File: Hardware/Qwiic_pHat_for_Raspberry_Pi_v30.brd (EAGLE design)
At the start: 65 x 30.5 mm, 46 parts, among them J1 RASPBERRYPI-40-PIN-GPIO_PTH_N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, J4 Qwiic Right Angle, J7 Qwiic Right Angle

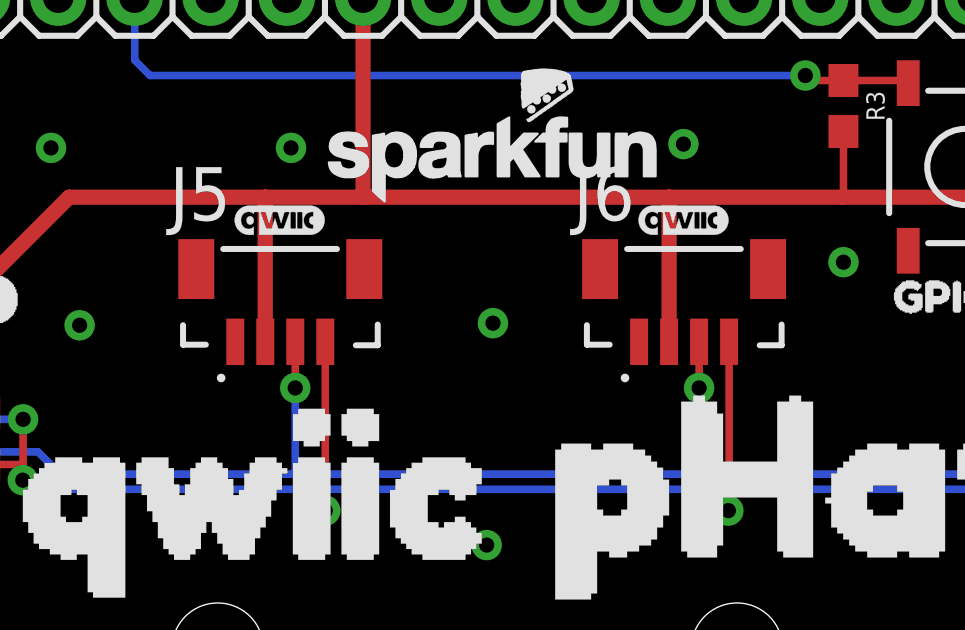
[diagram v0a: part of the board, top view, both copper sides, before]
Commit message: Fixes vertical qwiic connector polarity marker with updated package, removes Qwiic board reference on TDocu
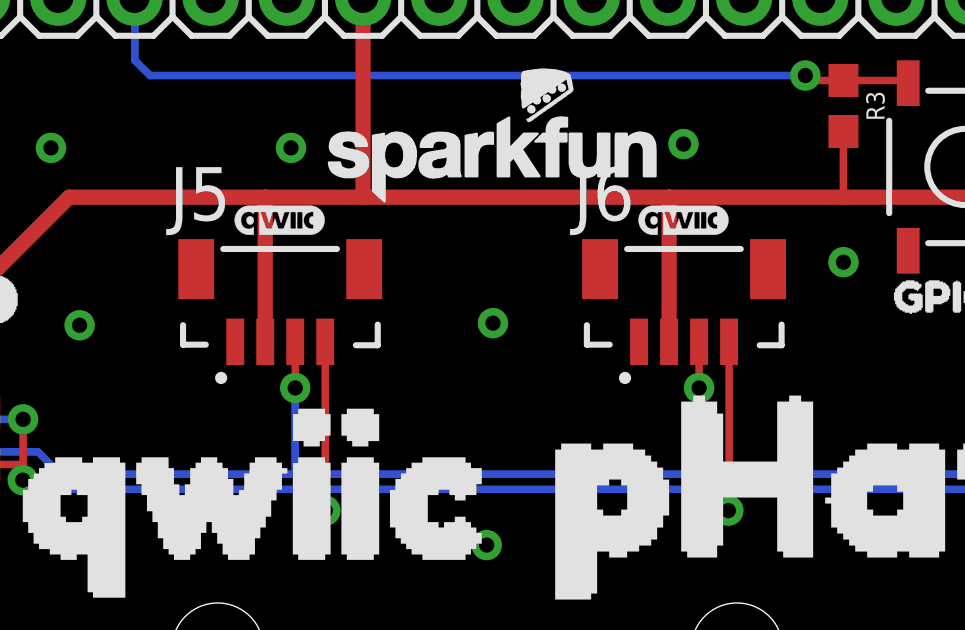
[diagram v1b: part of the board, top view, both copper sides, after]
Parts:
- removed U$4, U$5: (no value), SparkX:QWIIC_BOARD_MOUNT_NOHOLES
- moved LOGO1 16.7 mm to (9.91, -15.5)
- moved FRAME1 16.7 mm to (-1.52, -13.0)
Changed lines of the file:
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@@
 <wire x1="0" y1="27.5" x2="0" y2="3" width="0.2032" layer="20"/>
 <wire x1="0" y1="3" x2="3" y2="0" width="0.2032" layer="20" curve="90"/>
-<text x="24.638" y="-28.702" size="1.778" layer="51" font="vector">N. Seidle</text>
+<text x="30.226" y="-12.954" size="1.778" layer="51" font="vector">N. Seidle</text>
 <text x="55.771" y="0.818" size="1.27" layer="16" font="vector" ratio="15" rot="MR0">v30</text>
-<text x="23.368" y="-31.242" size="1.778" layer="51" font="vector">A. England and Elias Santistevan</text>
+<text x="28.956" y="-15.494" size="1.778" layer="51" font="vector">A. England and Elias Santistevan</text>
 <dimension x1="0" y1="30.5" x2="0" y2="0" x3="-5" y3="15.25" textsize="1.778" layer="47"/>
 <dimension x1="3.5" y1="26.5" x2="32.5" y2="26.5" x3="18" y3="32.5" textsize="1.778" layer="47"/>
@@
 </autorouter>
 <elements>
-<element name="FRAME1" library="SparkFun-Aesthetics" package="CREATIVE_COMMONS" value="FRAME-LETTER" x="-7.112" y="-28.702" smashed="yes">
-<attribute name="DESIGNER" value="" x="-7.112" y="-28.702" size="1.778" layer="27" display="off"/>
-<attribute name="REV" value="" x="-7.112" y="-28.702" size="1.778" layer="27" display="off"/>
+<element name="FRAME1" library="SparkFun-Aesthetics" package="CREATIVE_COMMONS" value="FRAME-LETTER" x="-1.524" y="-12.954" smashed="yes">
+<attribute name="DESIGNER" value="" x="-1.524" y="-12.954" size="1.778" layer="27" display="off"/>
+<attribute name="REV" value="" x="-1.524" y="-12.954" size="1.778" layer="27" display="off"/>
 </element>
 <element name="FD1" library="SparkFun-Aesthetics" package="FIDUCIAL-1X2" value="FIDUCIAL1X2" x="6.52" y="29.56" smashed="yes" rot="R180"/>
@@
 <element name="FD3" library="SparkFun-Aesthetics" package="FIDUCIAL-1X2" value="FIDUCIAL1X2" x="57.33" y="1.31" smashed="yes" rot="MR0"/>
 <element name="FD4" library="SparkFun-Aesthetics" package="FIDUCIAL-1X2" value="FIDUCIAL1X2" x="6.52" y="29.56" smashed="yes" rot="MR0"/>
-<element name="LOGO1" library="SparkFun-Aesthetics" package="REVISION" value="REVISION" x="4.318" y="-31.242" smashed="yes"/>
+<element name="LOGO1" library="SparkFun-Aesthetics" package="REVISION" value="REVISION" x="9.906" y="-15.494" smashed="yes"/>
 <element name="J1" library="SparkFun-Connectors" package="2X20" value="RASPBERRYPI-40-PIN-GPIO_PTH_NO_SHROUD" x="8.37" y="25.2" smashed="yes">
 <attribute name="NAME" x="7.1" y="29.264" size="0.6096" layer="25" font="vector" ratio="20"/>
@@
 </element>
 <element name="U$2" library="Labels" package="I2C-()" value="" x="13.2588" y="15.1384" smashed="yes"/>
-<element name="U$4" library="SparkX" package="QWIIC_BOARD_MOUNT_NOHOLES" value="" x="13.6906" y="-6.6802" smashed="yes"/>
-<element name="U$5" library="SparkX" package="QWIIC_BOARD_MOUNT_NOHOLES" value="" x="51.3334" y="-6.6802" smashed="yes"/>
 <element name="J3" library="SparkFun-Connectors" package="SCREWTERMINAL-3.5MM-2" value="" x="3.81" y="19.05" smashed="yes" rot="R270">
 <attribute name="NAME" x="6.35" y="20.32" size="0.6096" layer="25" font="vector" ratio="20" rot="R270"/>

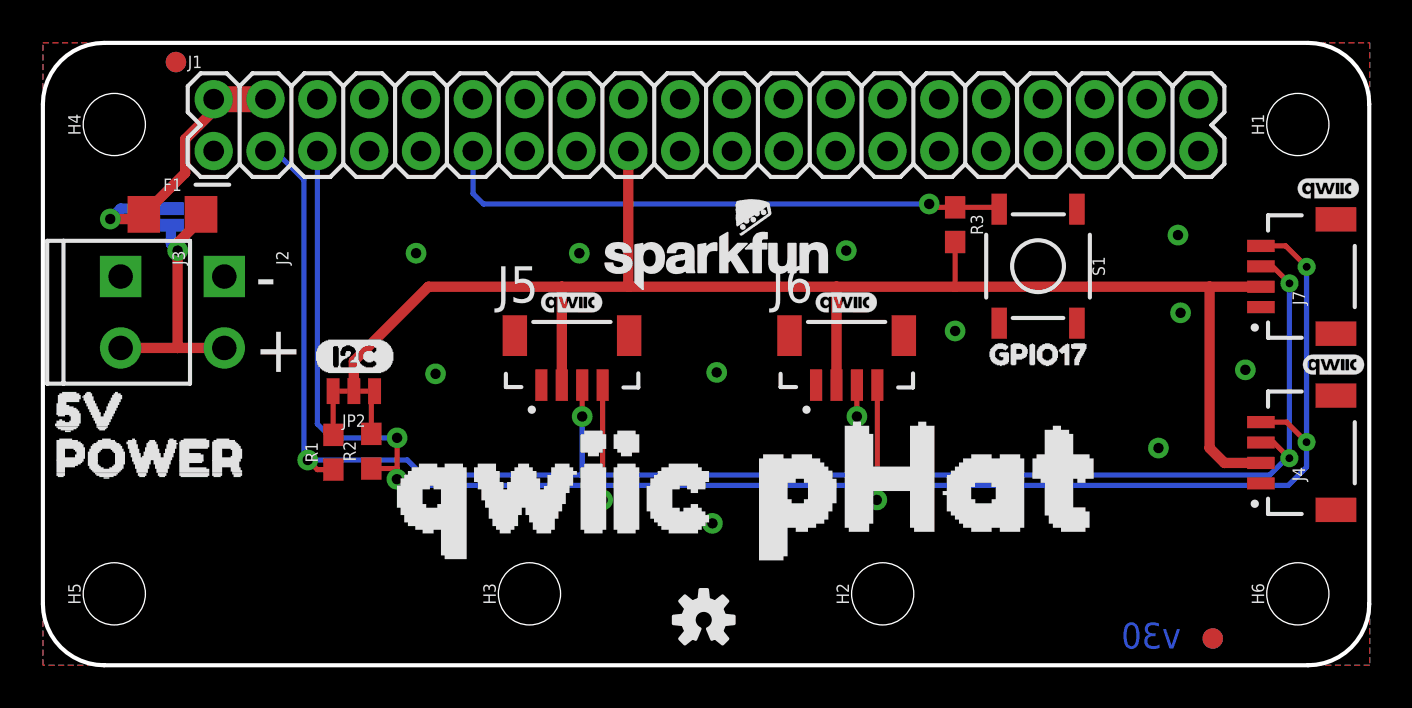
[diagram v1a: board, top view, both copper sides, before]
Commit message: Updates Vertical Qwiic connector to have value of "vertical qwiic connector"
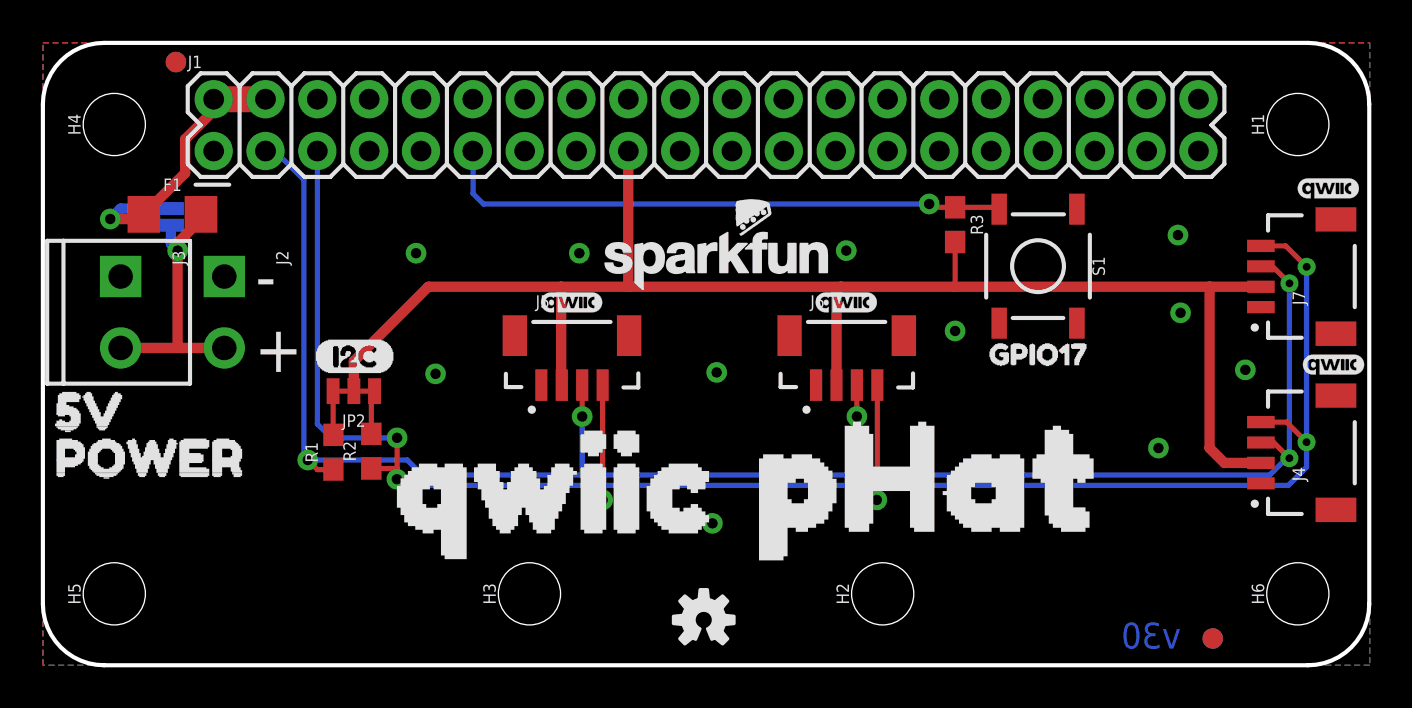
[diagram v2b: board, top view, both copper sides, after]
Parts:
- J5, J6: value (none) -> Vertical Qwiic Connector
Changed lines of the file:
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@@
 <layer number="115" name="ReferenceISLANDS" color="7" fill="1" visible="no" active="yes"/>
 <layer number="116" name="Patch_BOT" color="9" fill="4" visible="no" active="yes"/>
-<layer number="117" name="PM_Ref" color="26" fill="1" visible="yes" active="yes"/>
+<layer number="117" name="PM_Ref" color="26" fill="1" visible="no" active="yes"/>
 <layer number="118" name="Rect_Pads" color="7" fill="1" visible="no" active="yes"/>
-<layer number="119" name="PF_Ref" color="31" fill="1" visible="yes" active="yes"/>
-<layer number="120" name="WFL_Ref" color="25" fill="1" visible="yes" active="yes"/>
+<layer number="119" name="PF_Ref" color="31" fill="1" visible="no" active="yes"/>
+<layer number="120" name="WFL_Ref" color="25" fill="1" visible="no" active="yes"/>
 <layer number="121" name="_tsilk" color="7" fill="1" visible="no" active="yes"/>
 <layer number="122" name="_bsilk" color="7" fill="1" visible="no" active="yes"/>
@@
 <attribute name="VALUE" x="43.942" y="21.59" size="0.6096" layer="27" font="vector" ratio="20" rot="R270" align="top-center"/>
 </element>
-<element name="J5" library="SparkFun-Connectors" package="JST04_1MM_VERT" value="" x="24.13" y="12.954" smashed="yes">
-<attribute name="NAME" x="22.241" y="17.77433125" size="1.778" layer="25"/>
-<attribute name="PROD_ID" value="CONN-14483" x="24.13" y="12.954" size="1.778" layer="27" display="off"/>
-<attribute name="VALUE" x="22.241" y="10.13366875" size="1.778" layer="27"/>
-</element>
-<element name="J6" library="SparkFun-Connectors" package="JST04_1MM_VERT" value="" x="37.592" y="12.954" smashed="yes">
-<attribute name="NAME" x="35.703" y="17.77433125" size="1.778" layer="25"/>
-<attribute name="PROD_ID" value="CONN-14483" x="37.592" y="12.954" size="1.778" layer="27" display="off"/>
-<attribute name="VALUE" x="35.703" y="10.13366875" size="1.778" layer="27"/>
-</element>
 <element name="J2" library="SparkFun-Connectors" package="SCREWTERMINAL-3.5MM-2-NS" value="" x="8.89" y="19.05" smashed="yes" rot="R270">
 <attribute name="NAME" x="11.43" y="20.32" size="0.6096" layer="25" font="vector" ratio="20" rot="R270"/>
@@
 <element name="LOGO3" library="SparkFun-Aesthetics" package="SFE_LOGO_NAME_.1" value="SFE_LOGO_NAME.1_INCH" x="33.02" y="19.812" smashed="yes"/>
 <element name="U$10" library="SparkFun-Aesthetics" package="SFE_LOGO_NAME_FLAME_.3" value="" x="33.528" y="11.43" smashed="yes" rot="MR0"/>
+<element name="J5" library="SparkFun-Connectors" package="JST04_1MM_VERT" value="Vertical Qwiic Connector" x="24.13" y="12.954" smashed="yes">
+<attribute name="NAME" x="24.146" y="17.52033125" size="0.6096" layer="25"/>
+<attribute name="PROD_ID" value="CONN-14483" x="24.13" y="12.954" size="1.778" layer="27" font="vector" ratio="15" display="off"/>
+<attribute name="VALUE" x="24.146" y="11.65766875" size="0.6096" layer="27"/>
+</element>
+<element name="J6" library="SparkFun-Connectors" package="JST04_1MM_VERT" value="Vertical Qwiic Connector" x="37.592" y="12.954" smashed="yes">
+<attribute name="NAME" x="37.608" y="17.52033125" size="0.6096" layer="25"/>
+<attribute name="PROD_ID" value="CONN-14483" x="37.592" y="12.954" size="1.778" layer="27" font="vector" ratio="15" display="off"/>
+<attribute name="VALUE" x="37.608" y="11.65766875" size="0.6096" layer="27"/>
+</element>
 </elements>
 <signals>
@@
 <contactref element="J7" pad="1"/>
 <contactref element="J1" pad="6"/>
-<contactref element="J1" pad="9"/>
 <contactref element="J1" pad="14"/>
 <contactref element="J1" pad="20"/>
@@
 <via x="54.67" y="10.645" extent="1-16" drill="0.508"/>
 <contactref element="S1" pad="1"/>
-<contactref element="J6" pad="1"/>
-<contactref element="J5" pad="1"/>
 <contactref element="J3" pad="1"/>
 <contactref element="J2" pad="1"/>
+<contactref element="J1" pad="9"/>
+<contactref element="J5" pad="1"/>
+<contactref element="J6" pad="1"/>
 </signal>
 <signal name="3.3V">
@@
 <contactref element="R3" pad="2"/>
 <wire x1="57.1754" y1="18.55" x2="44.704" y2="18.55" width="0.508" layer="1"/>
-<wire x1="44.704" y1="18.55" x2="38.892" y2="18.55" width="0.508" layer="1"/>
-<wire x1="38.892" y1="18.55" x2="28.702" y2="18.55" width="0.508" layer="1"/>
-<wire x1="28.702" y1="18.55" x2="25.43" y2="18.55" width="0.508" layer="1"/>
+<wire x1="44.704" y1="18.55" x2="39.116" y2="18.55" width="0.508" layer="1"/>
+<wire x1="39.116" y1="18.55" x2="28.702" y2="18.55" width="0.508" layer="1"/>
 <wire x1="28.69" y1="18.562" x2="28.702" y2="18.55" width="0.508" layer="1"/>
 <wire x1="28.69" y1="25.2" x2="28.69" y2="18.562" width="0.508" layer="1"/>
 <wire x1="44.704" y1="20.74" x2="44.704" y2="18.55" width="0.254" layer="1"/>
-<contactref element="J5" pad="2"/>
-<contactref element="J6" pad="2"/>
-<wire x1="25.43" y1="13.729" x2="25.43" y2="18.55" width="0.508" layer="1"/>
-<wire x1="38.892" y1="13.729" x2="38.892" y2="18.55" width="0.508" layer="1"/>
-<wire x1="25.43" y1="18.55" x2="18.89115625" y2="18.55" width="0.508" layer="1"/>
+<wire x1="28.702" y1="18.55" x2="25.4" y2="18.55" width="0.508" layer="1"/>
 <contactref element="J7" pad="2"/>
+<wire x1="25.4" y1="18.55" x2="18.89115625" y2="18.55" width="0.508" layer="1"/>
 <wire x1="57.1754" y1="18.55" x2="59.69" y2="18.55" width="0.508" layer="1"/>
 <wire x1="15.2382" y1="14.89704375" x2="18.89115625" y2="18.55" width="0.508" layer="1"/>
 <wire x1="15.2382" y1="13.4348" x2="15.2382" y2="14.89704375" width="0.508" layer="1"/>
+<contactref element="J5" pad="2"/>
+<contactref element="J6" pad="2"/>
+<wire x1="39.116" y1="18.55" x2="38.892" y2="18.326" width="0.508" layer="1"/>
+<wire x1="38.892" y1="18.326" x2="38.892" y2="13.729" width="0.508" layer="1"/>
+<wire x1="25.43" y1="13.729" x2="25.4" y2="13.759" width="0.508" layer="1"/>
+<wire x1="25.4" y1="13.759" x2="25.4" y2="18.55" width="0.508" layer="1"/>
 </signal>
 <signal name="SDA">
@@
 <wire x1="12.9794" y1="10.0584" x2="17.8562" y2="10.0584" width="0.254" layer="16"/>
 <wire x1="17.8562" y1="10.0584" x2="18.5928" y2="9.3218" width="0.254" layer="16"/>
-<contactref element="J5" pad="3"/>
-<contactref element="J6" pad="3"/>
 <via x="26.43" y="12.192" extent="1-16" drill="0.508"/>
 <wire x1="26.43" y1="9.3218" x2="26.43" y2="9.398" width="0.254" layer="16"/>
@@
 <wire x1="14.2352" y1="9.5884" x2="13.4494" y2="9.5884" width="0.254" layer="1"/>
 <wire x1="13.4494" y1="9.5884" x2="12.9794" y2="10.0584" width="0.254" layer="1"/>
-<wire x1="26.43" y1="13.729" x2="26.43" y2="12.192" width="0.254" layer="1"/>
 <wire x1="26.43" y1="12.192" x2="26.43" y2="9.398" width="0.254" layer="16"/>
-<wire x1="39.892" y1="13.729" x2="39.892" y2="12.192" width="0.254" layer="1"/>
 <wire x1="39.892" y1="12.192" x2="39.892" y2="9.3358" width="0.254" layer="16"/>
 <wire x1="39.892" y1="9.3358" x2="39.878" y2="9.3218" width="0.254" layer="16"/>
@@
 <wire x1="12.7896" y1="10.2482" x2="12.7896" y2="23.7864" width="0.254" layer="16"/>
 <wire x1="12.7896" y1="23.7864" x2="11.376" y2="25.2" width="0.254" layer="16"/>
+<contactref element="J5" pad="3"/>
+<contactref element="J6" pad="3"/>
+<wire x1="39.892" y1="12.192" x2="39.892" y2="13.729" width="0.254" layer="1"/>
+<wire x1="26.43" y1="12.192" x2="26.43" y2="13.729" width="0.254" layer="1"/>
 </signal>
 <signal name="SCL">
@@
 <wire x1="61.926" y1="10.9332" x2="61.926" y2="9.7062" width="0.254" layer="16"/>
 <contactref element="R2" pad="1"/>
-<contactref element="J5" pad="4"/>
-<contactref element="J6" pad="4"/>
 <wire x1="27.432" y1="8.8138" x2="17.653" y2="8.8138" width="0.254" layer="16"/>
 <wire x1="17.3482" y1="9.1186" x2="17.653" y2="8.8138" width="0.254" layer="16"/>
-<wire x1="27.432" y1="8.1026" x2="27.43" y2="8.1046" width="0.254" layer="1"/>
-<wire x1="27.43" y1="13.729" x2="27.43" y2="8.1046" width="0.254" layer="1"/>
+<wire x1="27.43" y1="8.1046" x2="27.432" y2="8.1026" width="0.254" layer="1"/>
 <via x="27.432" y="8.1026" extent="1-16" drill="0.508"/>
 <wire x1="27.432" y1="8.1026" x2="27.432" y2="8.8138" width="0.254" layer="16"/>
 <via x="40.8666" y="8.1026" extent="1-16" drill="0.508"/>
-<wire x1="40.8666" y1="8.1026" x2="40.892" y2="8.128" width="0.254" layer="1"/>
-<wire x1="40.892" y1="13.729" x2="40.892" y2="8.128" width="0.254" layer="1"/>
 <wire x1="61.926" y1="9.7062" x2="61.0336" y2="8.8138" width="0.254" layer="16"/>
 <wire x1="61.0336" y1="8.8138" x2="40.894" y2="8.8138" width="0.254" layer="16"/>
@@
 <wire x1="16.096" y1="9.6392" x2="17.3452" y2="9.6392" width="0.254" layer="1"/>
 <wire x1="17.3452" y1="9.6392" x2="17.358" y2="9.652" width="0.254" layer="1"/>
+<contactref element="J5" pad="4"/>
+<contactref element="J6" pad="4"/>
+<wire x1="40.892" y1="13.729" x2="40.892" y2="8.128" width="0.254" layer="1"/>
+<wire x1="40.892" y1="8.128" x2="40.8666" y2="8.1026" width="0.254" layer="1"/>
+<wire x1="27.43" y1="13.729" x2="27.43" y2="8.1046" width="0.254" layer="1"/>
 </signal>
 <signal name="5V">
@@
 <wire x1="7.75" y1="21.847" x2="6.604" y2="20.701" width="0.508" layer="1"/>
 <contactref element="JP1" pad="2"/>
-<wire x1="6.2738" y1="21.5646" x2="6.2738" y2="21.5138" width="0.508" layer="16"/>
 <contactref element="J3" pad="2"/>
 <contactref element="J2" pad="2"/>
@@
 <wire x1="16.2542" y1="13.4348" x2="16.096" y2="13.2766" width="0.254" layer="1"/>
 <wire x1="16.096" y1="13.2766" x2="16.096" y2="11.3392" width="0.254" layer="1"/>
-</signal>
-<signal name="N$1">
-<contactref element="J1" pad="1"/>
 </signal>
 <signal name="N$2">
@@
 <wire x1="4.7214" y1="21.8694" x2="3.302" y2="21.8694" width="0.508" layer="1"/>
 </signal>
+<signal name="N$1">
+<contactref element="J1" pad="1"/>
+</signal>
 </signals>
